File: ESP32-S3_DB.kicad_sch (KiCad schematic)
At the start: 0 parts

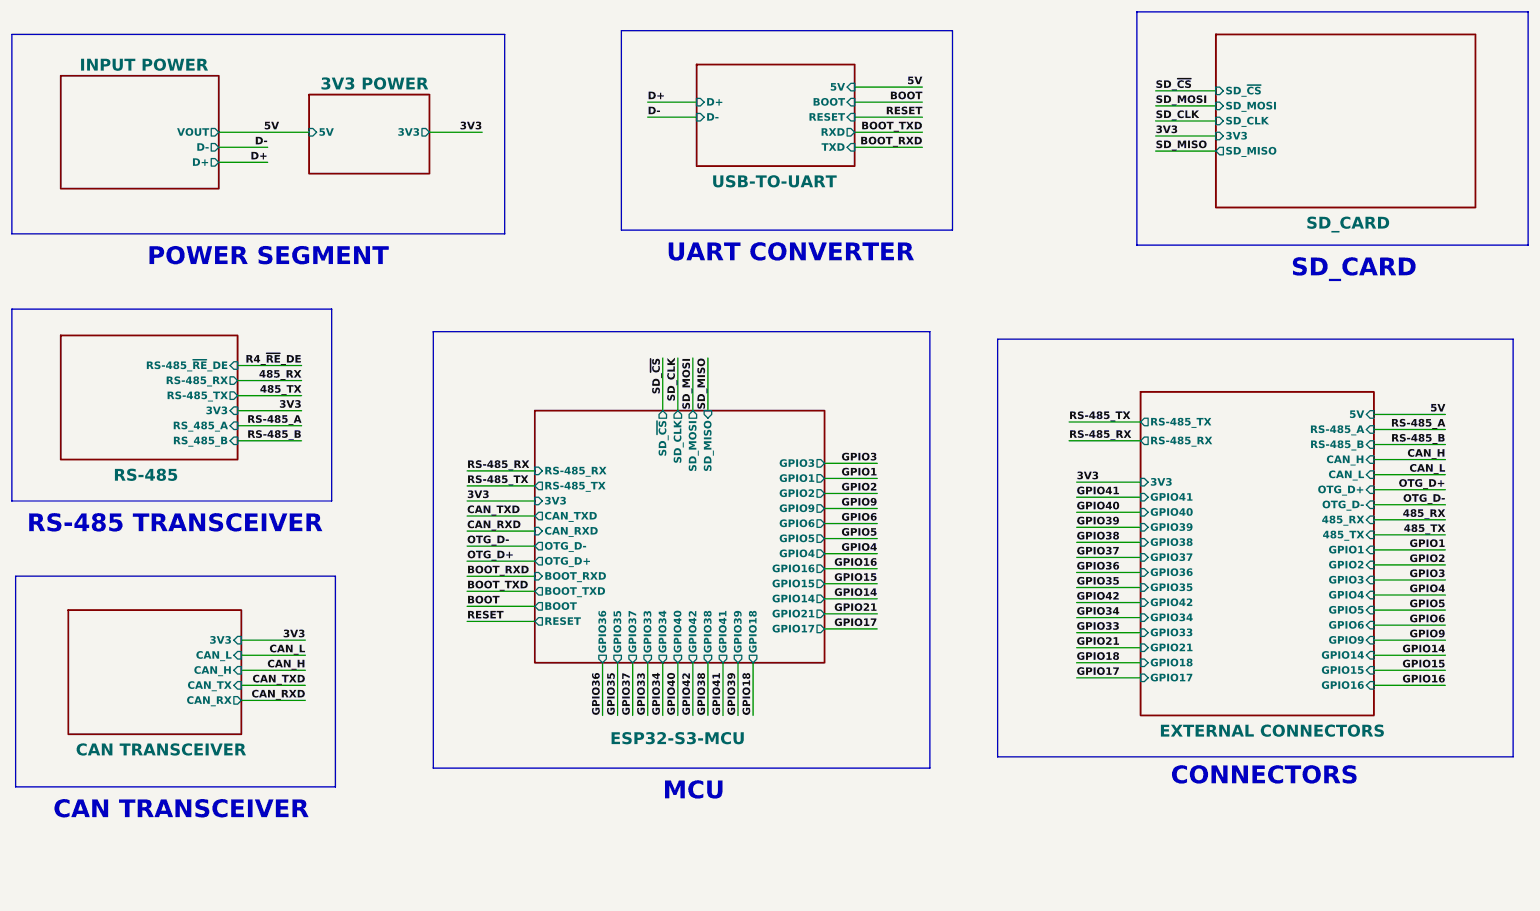
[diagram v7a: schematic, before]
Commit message: Completed header connections
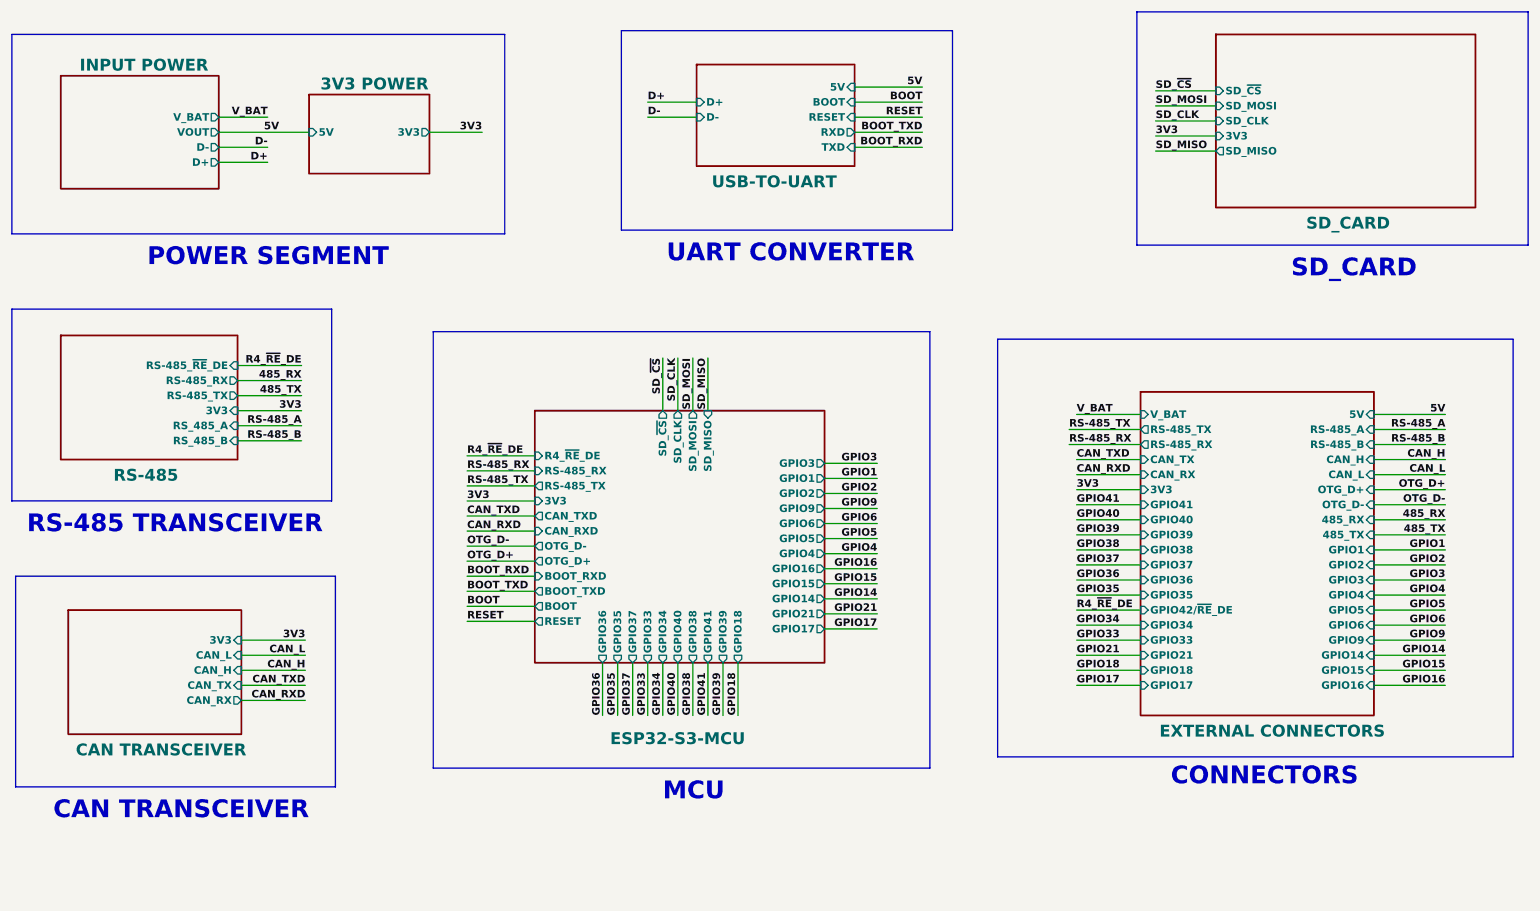
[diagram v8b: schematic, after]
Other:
- sheet ESP32-S3-MCU ports: added R4_~{RE}_DE; removed GPIO42
- sheet EXTERNAL CONNECTORS ports: added CAN_RX, CAN_TX, GPIO42/~{RE}_DE, V_BAT; removed GPIO42
- sheet INPUT POWER ports: added V_BAT; removed none
